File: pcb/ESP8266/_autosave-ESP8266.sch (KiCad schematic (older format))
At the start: 19 parts, among them J1 Conn_02x04, U1 ESP8266EX, U2 W25Q16BVSSIG

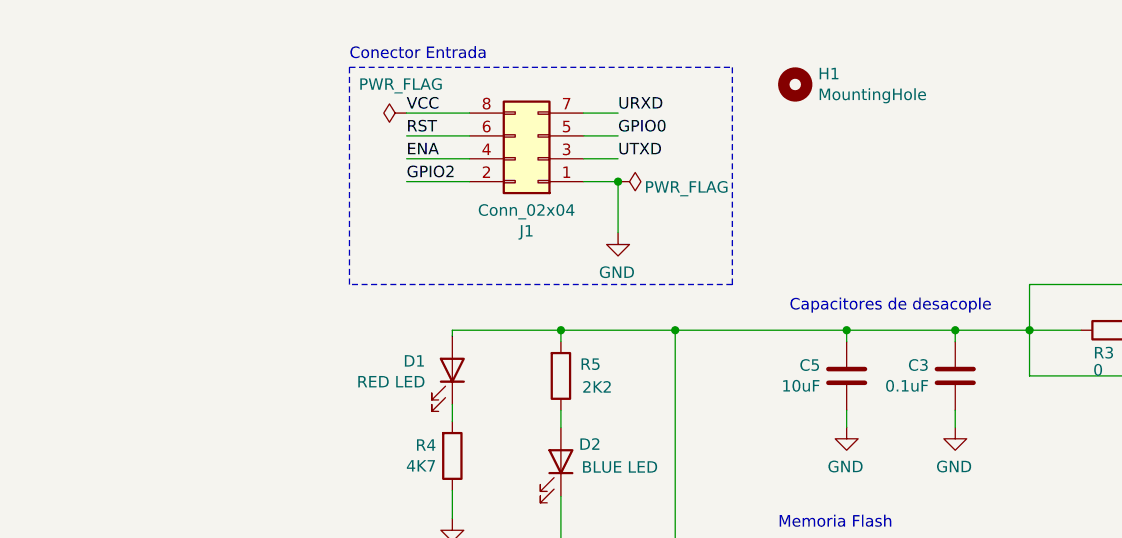
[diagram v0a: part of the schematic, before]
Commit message: agregado de modelos 3D al proeycto, fiduciales y agujero
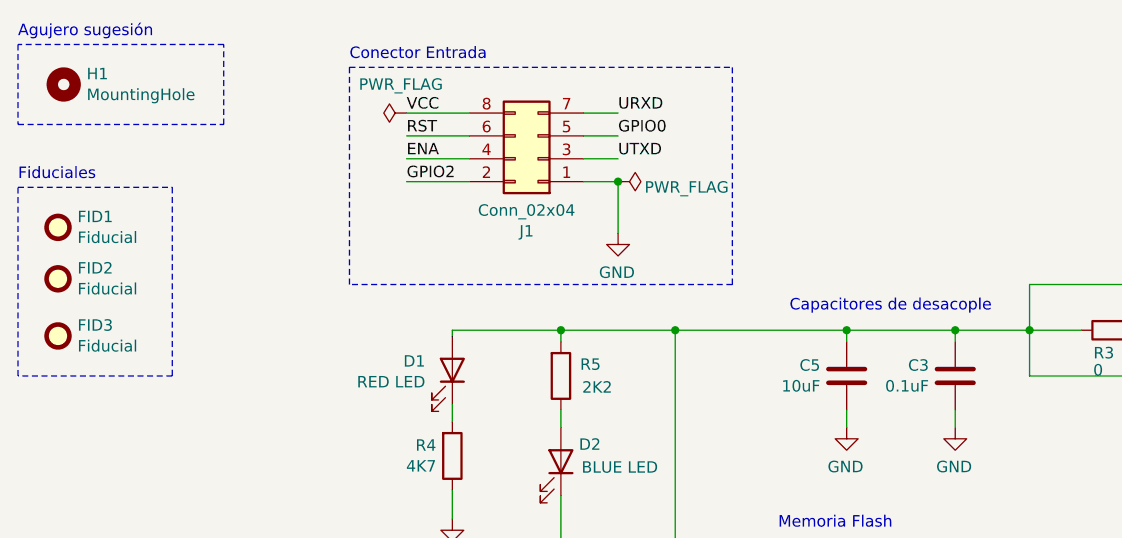
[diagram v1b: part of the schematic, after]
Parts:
- added FID1, FID2, FID3: Fiducial, Fiducial:Fiducial_1mm_Mask2mm, symbol Mechanical:Fiducial
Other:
- note added: "Agujero sugesión"
- note added: "Fiduciales"
- moved on the sheet: H1
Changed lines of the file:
@@
 L Mechanical:MountingHole H1
 U 1 1 5F8A9382
-P 4250 1625
-F 0 "H1" H 4350 1671 50  0000 L CNN
-F 1 "MountingHole" H 4350 1580 50  0000 L CNN
-F 2 "MountingHole:MountingHole_2mm" H 4250 1625 50  0001 C CNN
-F 3 "~" H 4250 1625 50  0001 C CNN
-	1    4250 1625
+P 1050 1625
+F 0 "H1" H 1150 1671 50  0000 L CNN
+F 1 "MountingHole" H 1150 1580 50  0000 L CNN
+F 2 "MountingHole:MountingHole_2mm" H 1050 1625 50  0001 C CNN
+F 3 "~" H 1050 1625 50  0001 C CNN
+	1    1050 1625
 	1    0    0    -1
 $EndComp
+$Comp
+L Mechanical:Fiducial FID1
+U 1 1 5F8B2921
+P 1025 2250
+F 0 "FID1" H 1110 2296 50  0000 L CNN
+F 1 "Fiducial" H 1110 2205 50  0000 L CNN
+F 2 "Fiducial:Fiducial_1mm_Mask2mm" H 1025 2250 50  0001 C CNN
+F 3 "~" H 1025 2250 50  0001 C CNN
+	1    1025 2250
+	1    0    0    -1
+$EndComp
+$Comp
+L Mechanical:Fiducial FID2
+U 1 1 5F8B46CF
+P 1025 2475
+F 0 "FID2" H 1110 2521 50  0000 L CNN
+F 1 "Fiducial" H 1110 2430 50  0000 L CNN
+F 2 "Fiducial:Fiducial_1mm_Mask2mm" H 1025 2475 50  0001 C CNN
+F 3 "~" H 1025 2475 50  0001 C CNN
+	1    1025 2475
+	1    0    0    -1
+$EndComp
+$Comp
+L Mechanical:Fiducial FID3
+U 1 1 5F8B4929
+P 1025 2725
+F 0 "FID3" H 1110 2771 50  0000 L CNN
+F 1 "Fiducial" H 1110 2680 50  0000 L CNN
+F 2 "Fiducial:Fiducial_1mm_Mask2mm" H 1025 2725 50  0001 C CNN
+F 3 "~" H 1025 2725 50  0001 C CNN
+	1    1025 2725
+	1    0    0    -1
+$EndComp
+Wire Notes Line
+	850  2075 1525 2075
+Wire Notes Line
+	1525 2075 1525 2900
+Wire Notes Line
+	1525 2900 850  2900
+Wire Notes Line
+	850  2900 850  2075
+Wire Notes Line
+	850  1450 850  1800
+Wire Notes Line
+	850  1800 1750 1800
+Wire Notes Line
+	1750 1800 1750 1450
+Wire Notes Line
+	1750 1450 850  1450
+Text Notes 850  1425 0    50   ~ 0
+Agujero sugesión
+Text Notes 850  2050 0    50   ~ 0
+Fiduciales
 $EndSCHEMATC
